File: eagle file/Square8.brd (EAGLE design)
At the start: 49.5 x 52.7 mm, 29 parts, among them J3 CR2032-172, U1 ATmega328mu, U2 CH340T, U3 CN3065, X1 16MHz, X2 12MHz

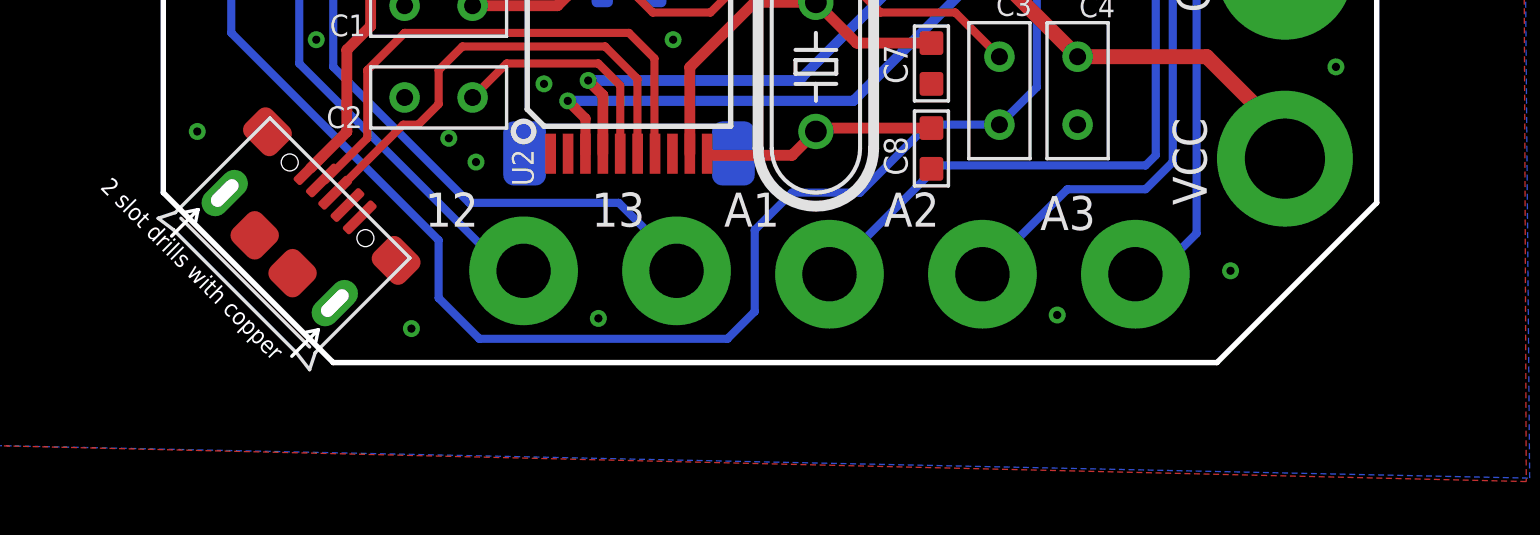
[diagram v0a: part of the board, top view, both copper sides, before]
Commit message: add github url to eagle file
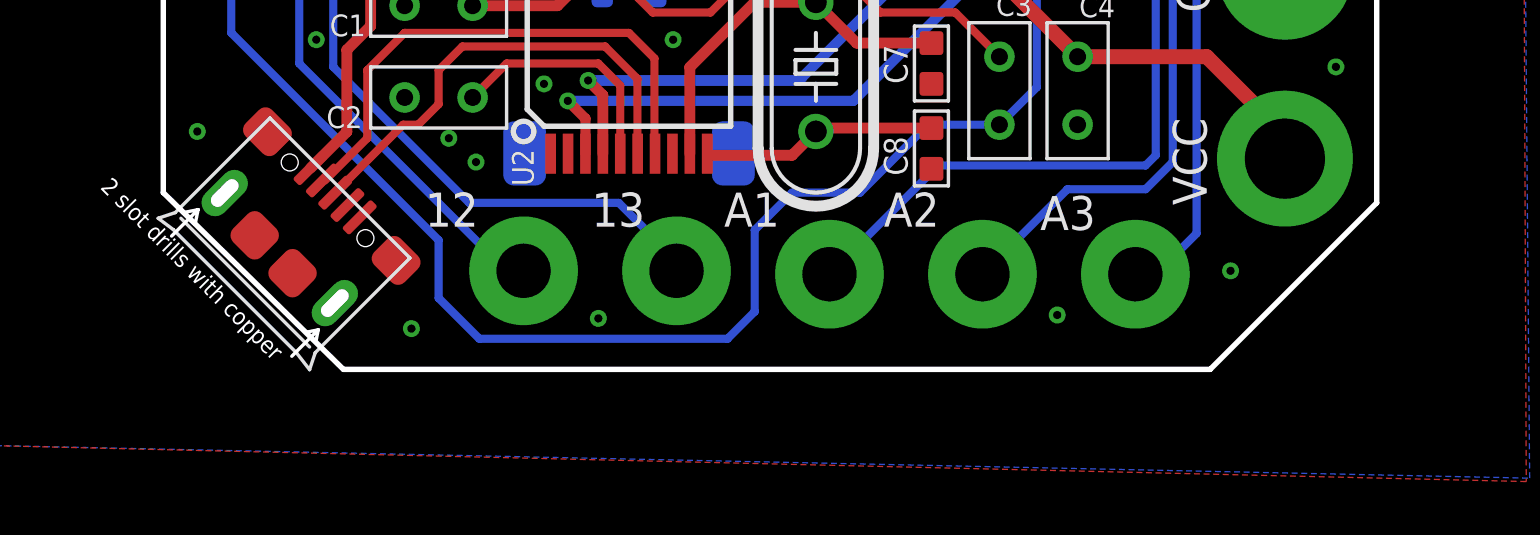
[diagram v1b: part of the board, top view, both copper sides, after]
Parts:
- moved U$1 1.20 mm to (28.1, 15.1)
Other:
- board size 49.5 x 52.7 mm -> 49.5 x 53 mm
- board text added: "https://github.com/loovee/Square8"
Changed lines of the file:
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@@
 <text x="7.874" y="31.369" size="1.27" layer="21" ratio="11" rot="R90">GND</text>
 <text x="43.561" y="6.731" size="1.27" layer="21" ratio="11" rot="R90">GND</text>
-<text x="34.798" y="22.987" size="2.54" layer="22" ratio="11" rot="MR0">8 SQUARE</text>
-<text x="34.671" y="20.447" size="1.27" layer="22" ratio="11" rot="MR0">V1.0 2014/4/10</text>
+<text x="34.29" y="28.956" size="2.54" layer="22" ratio="11" rot="MR0">8 SQUARE</text>
+<text x="34.29" y="26.797" size="1.27" layer="22" ratio="11" rot="MR0">V1.0 2014/4/10</text>
 <text x="12.446" y="10.541" size="0.889" layer="21" ratio="11">CHARGE STATE</text>
 <wire x1="38.735" y1="46.355" x2="5.08" y2="46.355" width="0.2032" layer="20"/>
@@
 <wire x1="49.784" y1="-0.381" x2="49.784" y2="16.256" width="0.2032" layer="20"/>
 <wire x1="0.254" y1="25.654" x2="0.254" y2="41.529" width="0.2032" layer="20"/>
-<wire x1="4.445" y1="0" x2="10.795" y2="-6.35" width="0.2032" layer="20"/>
-<wire x1="43.815" y1="-6.35" x2="10.795" y2="-6.35" width="0.2032" layer="20"/>
-<wire x1="43.815" y1="-6.35" x2="49.784" y2="-0.381" width="0.2032" layer="20"/>
+<wire x1="4.445" y1="0" x2="11.176" y2="-6.604" width="0.2032" layer="20"/>
+<wire x1="43.561" y1="-6.604" x2="11.176" y2="-6.604" width="0.2032" layer="20"/>
+<wire x1="43.561" y1="-6.604" x2="49.784" y2="-0.381" width="0.2032" layer="20"/>
 <wire x1="38.735" y1="46.355" x2="45.085" y2="40.005" width="0.2032" layer="20"/>
 <text x="37.211" y="-1.397" size="1.27" layer="25" ratio="11">A3</text>
@@
 <rectangle x1="25.908" y1="32.258" x2="32.512" y2="37.592" layer="30"/>
 <text x="10.795" y="29.21" size="1.778" layer="25" ratio="15">1</text>
+<text x="37.465" y="25.019" size="0.889" layer="26" ratio="11" rot="MR0">https://github.com/loovee/Square8</text>
 </plain>
 <attributes>
@@
 </element>
 <element name="J2" library="Connector " package="JST-SMD-2.0-90D" value="" x="21.846640625" y="3.645803125" rot="MR0"/>
-<element name="U$1" library="Logo" package="OSHW_FILLX200_NOTEXT" value="" x="28.448" y="13.97" rot="MR0"/>
+<element name="U$1" library="Logo" package="OSHW_FILLX200_NOTEXT" value="" x="28.067" y="15.113" rot="MR0"/>
 <element name="C2" library="Discrete" package="CERAMIC-2.54" value="100nF" x="14.732" y="3.556" smashed="yes">
 <attribute name="NAME" x="10.541" y="2.413" size="0.8128" layer="25" ratio="10"/>

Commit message: add an two-dimension code to pcb
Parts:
- moved U$1 50.8 mm to (31.2, 65.8)
- moved U2 27.4 mm to (25.0, 32.3)
- moved U3 27.4 mm to (13.2, 62.1)
- moved X1 27.4 mm to (30.5, 48.9)
- moved C2 27.4 mm to (17.9, 30.7)
- moved C3 27.4 mm to (38.9, 31.0)
- moved C4 27.4 mm to (41.8, 31.0)
- moved C6 27.4 mm to (34.9, 52.5)
- moved C8 27.4 mm to (36.3, 28.8)
- moved J1 27.4 mm to (14.2, 27.4)
- moved J2 27.4 mm to (25.0, 30.8)
- moved R1 27.4 mm to (17.1, 50.2)
- moved R2 27.4 mm to (19.5, 50.2)
- moved R3 27.4 mm to (21.8, 50.2)
- moved C1 27.4 mm to (17.9, 34.2)
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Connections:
- net GND: now also J1.S4, J1.S5, J1.S6
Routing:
- net N$6: track 0.00 -> 1.94 mm
- net ROW3: track 14.5 -> 16.1 mm
- net N$11: track 0.00 -> 1.48 mm
- net ROW2: track 18.5 -> 19.9 mm
- net ROW1: track 21.8 -> 23.3 mm
- net N$71: track 0.00 -> 1.27 mm
- net N$68: track 0.00 -> 1.14 mm
- net N$70: track 0.00 -> 1.14 mm
- net COL6: track 17.3 -> 18.4 mm
- net N$74: track 0.00 -> 1.02 mm
- net N$72: track 0.00 -> 1.02 mm
- net N$67: track 0.00 -> 1.02 mm
- net N$38: track 0.00 -> 1.02 mm
- net COL2: track 33.3 -> 34.2 mm
- net N$73: track 0.00 -> 0.89 mm
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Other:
- board text added: "V1.1 2014/4/19"
- board text removed: "V1.0 2014/4/10"
